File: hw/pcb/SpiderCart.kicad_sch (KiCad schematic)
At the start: 58 parts, among them J1 GameBoy_Cartridge, J2 USB_C_Receptacle_USB2.0_16P, J4 Conn_01x03, J5 Conn_01x02, J6 TF-01A, Q1 AO3401A, U1 RP2354B, U10 LIS3DH, U2 NCP1117-3.3_SOT223, U4 TXS0108EPW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

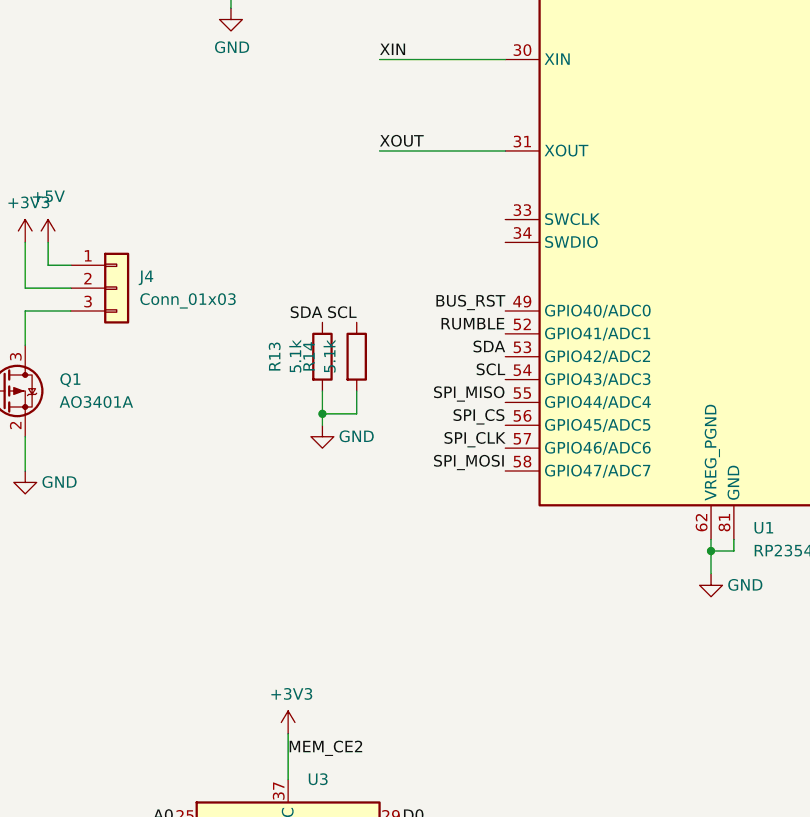
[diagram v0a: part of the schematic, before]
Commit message: Add I2C extension pins, and SWD pins
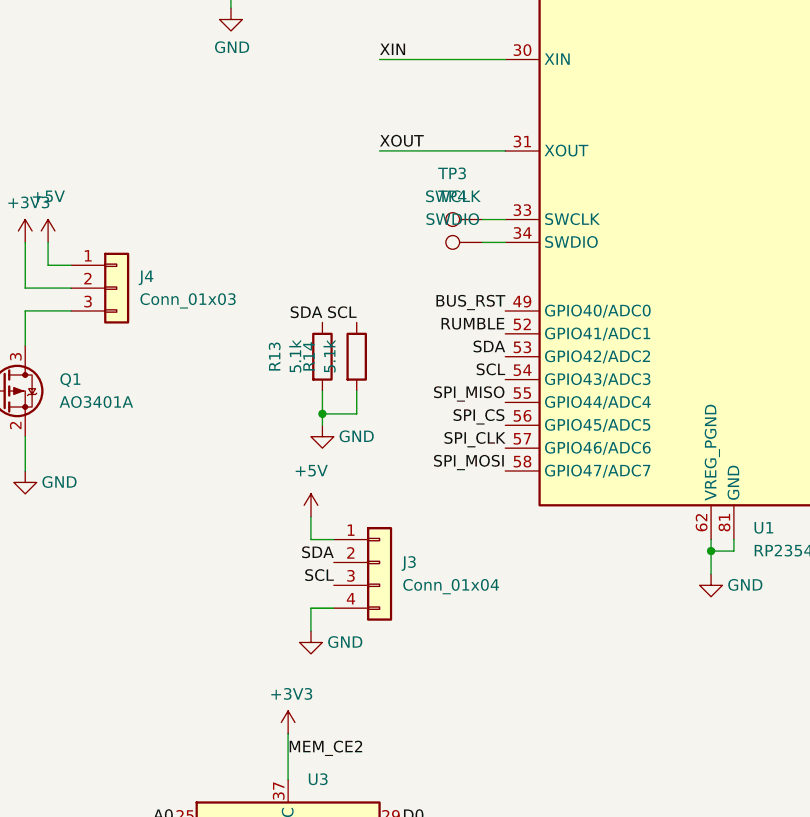
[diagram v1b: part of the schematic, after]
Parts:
- added J3: Conn_01x04, Connector_PinHeader_1.27mm:PinHeader_1x04_P1.27mm_Vertical, symbol Connector_Generic:Conn_01x04
- added TP3: SWCLK, TestPoint:TestPoint_Pad_D1.5mm, symbol Connector:TestPoint
- added TP4: SWDIO, TestPoint:TestPoint_Pad_D1.5mm, symbol Connector:TestPoint
- J1, J4, J5, TP1, TP2: now left out of the parts list
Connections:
- net +5V: now also J3.1 (Pin_1)
- net GND: now also J3.4 (Pin_4)
- net SCL: now also J3.3 (Pin_3)
- net SDA: now also J3.2 (Pin_2)
- net at U1.33 (SWCLK): now also TP3.1
- net at U1.34 (SWDIO): now also TP4.1

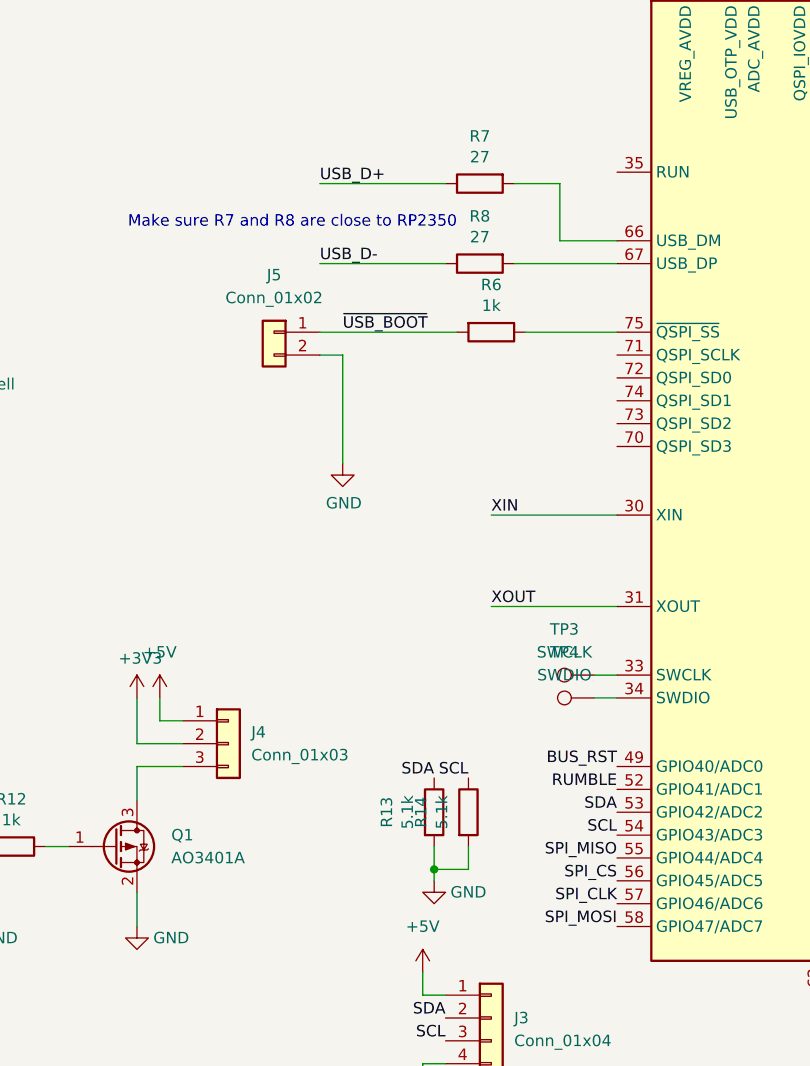
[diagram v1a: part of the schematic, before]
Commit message: Correct issues found in V1 production. I2C pullups where pulldowns, USB D- and D+ where swapped.
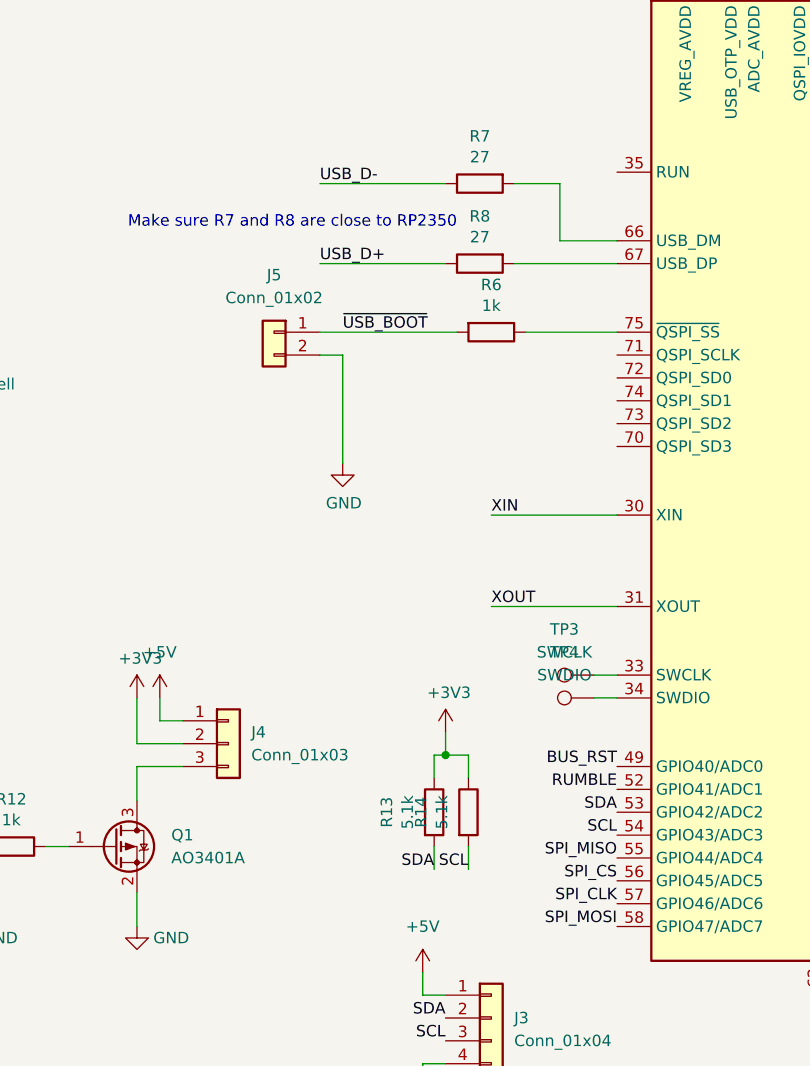
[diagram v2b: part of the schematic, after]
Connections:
- net +3V3: now also R13.1, R14.1
- net GND: no longer R13.2, R14.2
- net SCL: now also R14.2; no longer R14.1
- net SDA: now also R13.2; no longer R13.1
- net USB_D+: now also R8.1; no longer R7.1
- net USB_D-: now also R7.1; no longer R8.1
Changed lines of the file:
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@@
 	)
 	(junction
-		(at 256.54 158.75)
-		(diameter 0)
-		(color 0 0 0 0)
-	)
-	(junction
 		(at 378.46 19.05)
 		(diameter 0)
@@
 	)
 	(junction
+		(at 257.81 146.05)
+		(diameter 0)
+		(color 0 0 0 0)
+	)
+	(junction
 		(at 62.23 265.43)
 		(diameter 0)
@@
 	(wire
 		(pts
+			(xy 256.54 146.05) (xy 257.81 146.05)
+		)
+		(stroke
+			(width 0)
+			(type default)
+		)
+	)
+	(wire
+		(pts
+			(xy 260.35 146.05) (xy 260.35 148.59)
+		)
+		(stroke
+			(width 0)
+			(type default)
+		)
+	)
+	(wire
+		(pts
 			(xy 72.39 135.89) (xy 72.39 119.38)
 		)
@@
 	(wire
 		(pts
-			(xy 256.54 158.75) (xy 256.54 160.02)
-		)
-		(stroke
-			(width 0)
-			(type default)
-		)
-	)
-	(wire
-		(pts
 			(xy 90.17 128.27) (xy 80.01 128.27)
 		)
@@
 	(wire
 		(pts
-			(xy 256.54 156.21) (xy 256.54 158.75)
-		)
-		(stroke
-			(width 0)
-			(type default)
-		)
-	)
-	(wire
-		(pts
 			(xy 62.23 52.07) (xy 62.23 86.36)
 		)
@@
 	(wire
 		(pts
+			(xy 256.54 158.75) (xy 256.54 156.21)
+		)
+		(stroke
+			(width 0)
+			(type default)
+		)
+	)
+	(wire
+		(pts
 			(xy 307.34 49.53) (xy 307.34 58.42)
 		)
@@
 	(wire
 		(pts
-			(xy 256.54 158.75) (xy 260.35 158.75)
+			(xy 257.81 143.51) (xy 257.81 146.05)
 		)
 		(stroke
@@
 	(wire
 		(pts
-			(xy 260.35 156.21) (xy 260.35 158.75)
-		)
-		(stroke
-			(width 0)
-			(type default)
-		)
-	)
-	(wire
-		(pts
 			(xy 54.61 179.07) (xy 54.61 137.16)
 		)
@@
 	(wire
 		(pts
+			(xy 256.54 148.59) (xy 256.54 146.05)
+		)
+		(stroke
+			(width 0)
+			(type default)
+		)
+	)
+	(wire
+		(pts
 			(xy 346.71 43.18) (xy 346.71 41.91)
 		)
@@
 	(wire
 		(pts
+			(xy 257.81 146.05) (xy 260.35 146.05)
+		)
+		(stroke
+			(width 0)
+			(type default)
+		)
+	)
+	(wire
+		(pts
 			(xy 36.83 265.43) (xy 26.67 265.43)
 		)
@@
 	(wire
 		(pts
+			(xy 260.35 158.75) (xy 260.35 156.21)
+		)
+		(stroke
+			(width 0)
+			(type default)
+		)
+	)
+	(wire
+		(pts
 			(xy 72.39 87.63) (xy 90.17 87.63)
 		)
@@
 		)
 	)
+	(label "USB_D-"
+		(at 243.84 82.55 0)
+		(effects
+			(font
+				(size 1.27 1.27)
+			)
+			(justify left bottom)
+		)
+	)
 	(label "A8"
 		(at 240.03 224.79 180)
@@
 	)
 	(label "SDA"
-		(at 256.54 148.59 180)
+		(at 256.54 158.75 180)
 		(effects
 			(font
@@
 		)
 	)
-	(label "USB_D+"
-		(at 243.84 82.55 0)
-		(effects
-			(font
-				(size 1.27 1.27)
-			)
-			(justify left bottom)
-		)
-	)
 	(label "SCL"
 		(at 180.34 107.95 0)
@@
 	)
 	(label "SCL"
-		(at 260.35 148.59 180)
+		(at 260.35 158.75 180)
 		(effects
 			(font
@@
 		)
 	)
-	(label "USB_D-"
-		(at 243.84 91.44 0)
-		(effects
-			(font
-				(size 1.27 1.27)
-			)
-			(justify left bottom)
-		)
-	)
 	(label "MCB_A1"
 		(at 240.03 242.57 180)
@@
 		)
 	)
+	(label "USB_D+"
+		(at 243.84 91.44 0)
+		(effects
+			(font
+				(size 1.27 1.27)
+			)
+			(justify left bottom)
+		)
+	)
 	(label "A5"
 		(at 110.49 80.01 0)
@@
 	)
 	(symbol
+		(lib_id "power:+3V3")
+		(at 257.81 143.51 0)
+		(unit 1)
+		(body_style 1)
+		(exclude_from_sim no)
+		(in_bom yes)
+		(on_board yes)
+		(in_pos_files yes)
+		(dnp no)
+		(property "Reference" "#PWR058"
+			(at 257.81 147.32 0)
+			(hide yes)
+			(show_name no)
+			(do_not_autoplace no)
+			(effects
+				(font
+					(size 1.27 1.27)
+				)
+			)
+		)
+		(property "Value" "+3V3"
+			(at 258.191 139.1158 0)
+			(show_name no)
+			(do_not_autoplace no)
+			(effects
+				(font
+					(size 1.27 1.27)
+				)
+			)
+		)
+		(property "Footprint" ""
+			(at 257.81 143.51 0)
+			(hide yes)
+			(show_name no)
+			(do_not_autoplace no)
+			(effects
+				(font
+					(size 1.27 1.27)
+				)
+			)
+		)
+		(property "Datasheet" ""
+			(at 257.81 143.51 0)
+			(hide yes)
+			(show_name no)
+			(do_not_autoplace no)
+			(effects
+				(font
+					(size 1.27 1.27)
+				)
+			)
+		)
+		(property "Description" ""
+			(at 257.81 143.51 0)
+			(show_name no)
+			(do_not_autoplace no)
+			(effects
+				(font
+					(size 1.27 1.27)
+				)
+			)
+		)
+		(pin "1"
+		)
+		(instances
+			(project "SpiderCart"
+				(path "/e2f315fa-14d3-4a59-a530-3af717ade5b5"
+					(reference "#PWR058")
+					(unit 1)
+				)
+			)
+		)
+	)
+	(symbol
 		(lib_id "Device:R")
 		(at 209.55 156.21 270)
@@
 					(unit 1)
 				)
-			)
-		)
-	)
-	(symbol
-		(lib_id "power:GND")
-		(at 256.54 160.02 0)
-		(mirror y)
-		(unit 1)
-		(body_style 1)
-		(exclude_from_sim no)
-		(in_bom yes)
-		(on_board yes)
-		(in_pos_files yes)
-		(dnp no)
-		(property "Reference" "#PWR058"
-			(at 256.54 166.37 0)
-			(hide yes)
-			(show_name no)
-			(do_not_autoplace no)
-			(effects
-				(font
-					(size 1.27 1.27)
-				)
-			)
-		)
-		(property "Value" "GND"
-			(at 260.35 161.29 0)
-			(show_name no)
-			(do_not_autoplace no)
-			(effects
-				(font
-					(size 1.27 1.27)
-				)
-			)
-		)
-		(property "Footprint" ""
-			(at 256.54 160.02 0)
-			(hide yes)
-			(show_name no)
-			(do_not_autoplace no)
-			(effects
-				(font
-					(size 1.27 1.27)
-				)
-			)
-		)
-		(property "Datasheet" ""
-			(at 256.54 160.02 0)
-			(hide yes)
-			(show_name no)
-			(do_not_autoplace no)
-			(effects
-				(font
-					(size 1.27 1.27)
-				)
-			)
-		)
-		(property "Description" ""
-			(at 256.54 160.02 0)
-			(show_name no)
-			(do_not_autoplace no)
-			(effects
-				(font
-					(size 1.27 1.27)
-				)
-			)
-		)
-		(pin "1"
-		)
-		(instances
-			(project "SpiderCart"
-				(path "/e2f315fa-14d3-4a59-a530-3af717ade5b5"
-					(reference "#PWR058")
-					(unit 1)
-				)

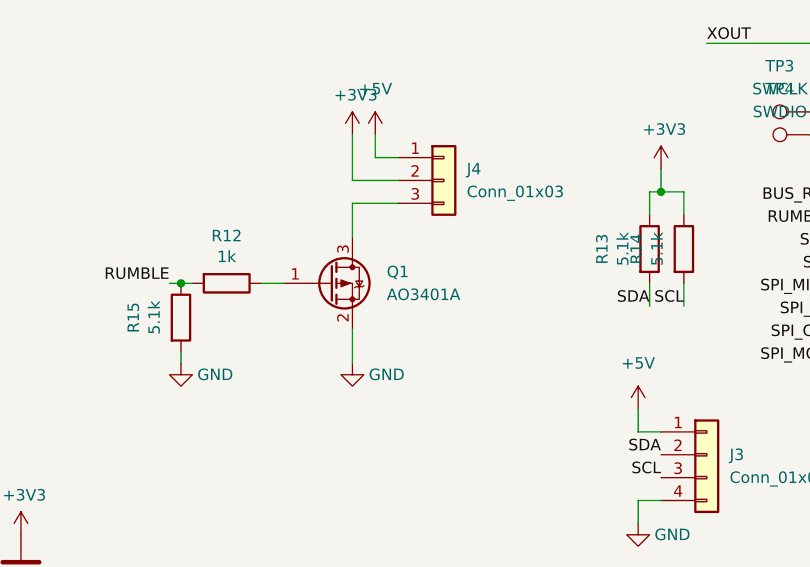
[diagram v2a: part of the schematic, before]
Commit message: Fix the wrong FET in V1 design
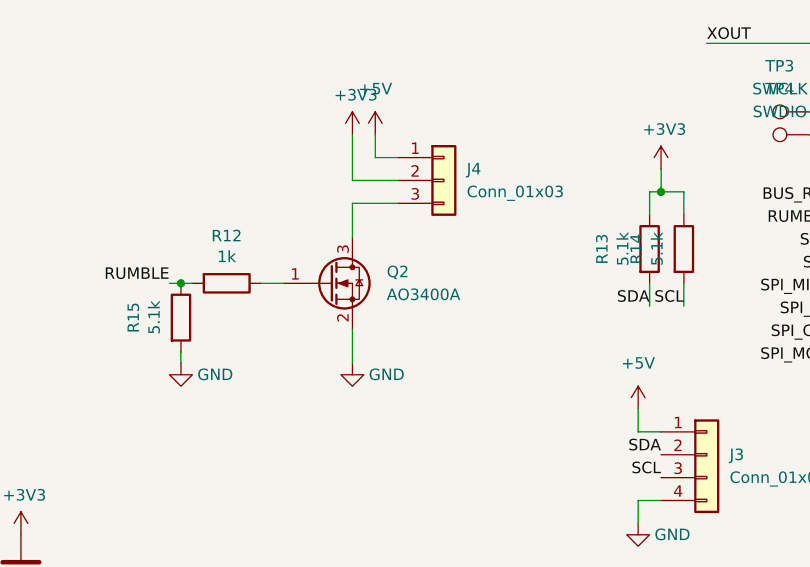
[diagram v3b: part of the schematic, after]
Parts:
- removed Q1: AO3401A, Package_TO_SOT_SMD:SOT-23, symbol Transistor_FET:AO3401A
- added Q2: AO3400A, Package_TO_SOT_SMD:SOT-23, symbol Transistor_FET:AO3400A
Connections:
- net GND: now also Q2.2 (S)
- net at J4.3 (Pin_3): now also Q2.3 (D)
- net at R12.1: now also Q2.1 (G)
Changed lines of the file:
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@@
-	)
-	(symbol
-		(lib_id "Transistor_FET:AO3401A")
-		(at 220.98 156.21 0)
-		(unit 1)
-		(body_style 1)
-		(exclude_from_sim no)
-		(in_bom yes)
-		(on_board yes)
-		(in_pos_files yes)
-		(dnp no)
-		(fields_autoplaced yes)
-		(property "Reference" "Q1"
-			(at 227.33 154.9399 0)
-			(show_name no)
-			(do_not_autoplace no)
-			(effects
-				(font
-					(size 1.27 1.27)
-				)
-				(justify left)
-			)
-		)
-		(property "Value" "AO3401A"
-			(at 227.33 157.4799 0)
-			(show_name no)
-			(do_not_autoplace no)
-			(effects
-				(font
-					(size 1.27 1.27)
-				)
-				(justify left)
-			)
-		)
-		(property "Footprint" "Package_TO_SOT_SMD:SOT-23"
-			(at 226.06 158.115 0)
-			(hide yes)
-			(show_name no)
-			(do_not_autoplace no)
-			(effects
-				(font
-					(size 1.27 1.27)
-					(italic yes)
-				)
-				(justify left)
-			)
-		)
-		(property "Datasheet" "http://www.aosmd.com/pdfs/datasheet/AO3401A.pdf"
-			(at 226.06 160.02 0)
-			(hide yes)
-			(show_name no)
-			(do_not_autoplace no)
-			(effects
-				(font
-					(size 1.27 1.27)
-				)
-				(justify left)
-			)
-		)
-		(property "Description" "-4.0A Id, -30V Vds, P-Channel MOSFET, SOT-23"
-			(at 220.98 156.21 0)
-			(hide yes)
-			(show_name no)
-			(do_not_autoplace no)
-			(effects
-				(font
-					(size 1.27 1.27)
-				)
-			)
-		)
-		(pin "2"
-		)
-		(pin "1"
-		)
-		(pin "3"
-		)
-		(instances
-			(project "SpiderCart"
-				(path "/e2f315fa-14d3-4a59-a530-3af717ade5b5"
-					(reference "Q1")
-					(unit 1)
-				)
-			)
-		)
 	)
 	(symbol
@@
 					(unit 1)
 				)
+			)
+		)
+	)
+	(symbol
+		(lib_id "Transistor_FET:AO3400A")
+		(at 220.98 156.21 0)
+		(unit 1)
+		(body_style 1)
+		(exclude_from_sim no)
+		(in_bom yes)
+		(on_board yes)
+		(in_pos_files yes)
+		(dnp no)
+		(fields_autoplaced yes)
+		(property "Reference" "Q2"
+			(at 227.33 154.9399 0)
+			(show_name no)
+			(do_not_autoplace no)
+			(effects
+				(font
+					(size 1.27 1.27)
+				)
+				(justify left)
+			)
+		)
+		(property "Value" "AO3400A"
+			(at 227.33 157.4799 0)
+			(show_name no)
+			(do_not_autoplace no)
+			(effects
+				(font
+					(size 1.27 1.27)
+				)
+				(justify left)
+			)
+		)
+		(property "Footprint" "Package_TO_SOT_SMD:SOT-23"
+			(at 226.06 158.115 0)
+			(hide yes)
+			(show_name no)
+			(do_not_autoplace no)
+			(effects
+				(font
+					(size 1.27 1.27)
+					(italic yes)
+				)
+				(justify left)
+			)
+		)
+		(property "Datasheet" "http://www.aosmd.com/pdfs/datasheet/AO3400A.pdf"
+			(at 226.06 160.02 0)
+			(hide yes)
+			(show_name no)
+			(do_not_autoplace no)
+			(effects
+				(font
+					(size 1.27 1.27)
+				)
+				(justify left)
+			)
+		)
+		(property "Description" "30V Vds, 5.7A Id, N-Channel MOSFET, SOT-23"
+			(at 220.98 156.21 0)
+			(hide yes)
+			(show_name no)
+			(do_not_autoplace no)
+			(effects
+				(font
+					(size 1.27 1.27)
+				)
+			)
+		)
+		(pin "2"
+		)
+		(pin "1"
+		)
+		(pin "3"
+		)
+		(instances
+			(project "SpiderCart"
+				(path "/e2f315fa-14d3-4a59-a530-3af717ade5b5"
+					(reference "Q2")
+					(unit 1)
+				)
